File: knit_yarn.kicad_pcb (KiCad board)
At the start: 2 copper layers, 33.8 x 36.1 mm, 10 parts, among them SW1 SW_SPST

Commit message: components in place
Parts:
- added D5: LED, LED_SMD:LED_0603_1608Metric_Pad1.05x0.95mm_HandSolder, B.Cu at (107.4, 80.2)
- added D6: LED, LED_SMD:LED_0603_1608Metric_Pad1.05x0.95mm_HandSolder, B.Cu at (91.6, 80.5)
- added R5: TBD, Resistor_SMD:R_0603_1608Metric_Pad0.98x0.95mm_HandSolder, B.Cu at (110.0, 81.2)
- added R6: TBD, Resistor_SMD:R_0603_1608Metric_Pad0.98x0.95mm_HandSolder, B.Cu at (89.0, 81.5)
- D1, D2, D3, D4, R1, R2, R3, R4: moved to B.Cu
- moved R4 52.7 mm to (85.0, 86.5), turned to 90 degrees
- moved R2 52.1 mm to (85.0, 90.0), turned to -90 degrees
- moved D4 48.7 mm to (87.0, 75.5), turned to -135 degrees
- moved D2 46.8 mm to (88.2, 104.0), turned to 45 degrees
- moved D3 27.6 mm to (111.9, 74.1), turned to -45 degrees
- moved D1 25.7 mm to (112.6, 103.0), turned to 135 degrees
- moved R3 23.7 mm to (114.5, 84.8), turned to 90 degrees
- moved R1 22.6 mm to (114.5, 88.2), turned to -90 degrees
- moved SW1 2.00 mm to (99.5, 77.0)
- moved BT1 0.25 mm to (111.9, 93.8)
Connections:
- BT1 pad 1: +3V0 -> Net-(BT1-+)
- SW1 pad 1: unconnected-(SW1-A-Pad1) -> Net-(BT1-+)
- SW1 pad 2: unconnected-(SW1-B-Pad2) -> +3V0

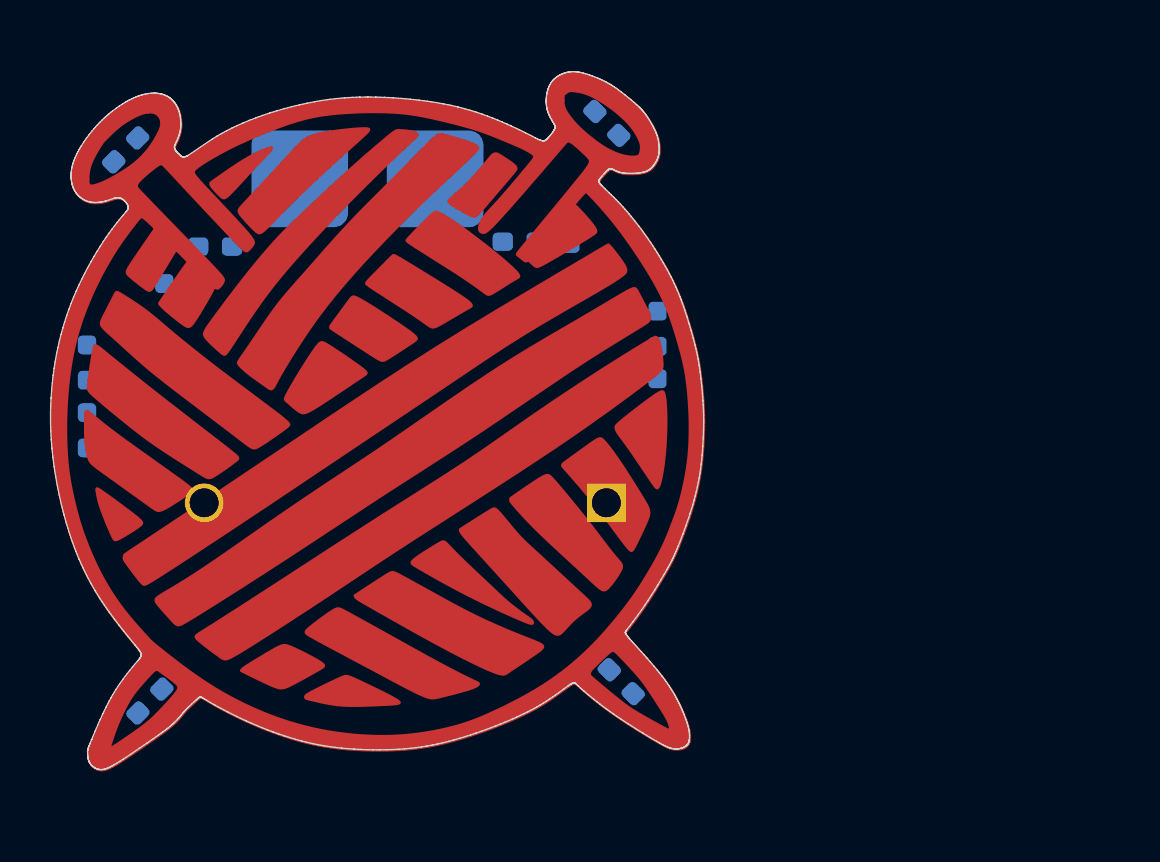
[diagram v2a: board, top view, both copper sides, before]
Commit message: back pour area
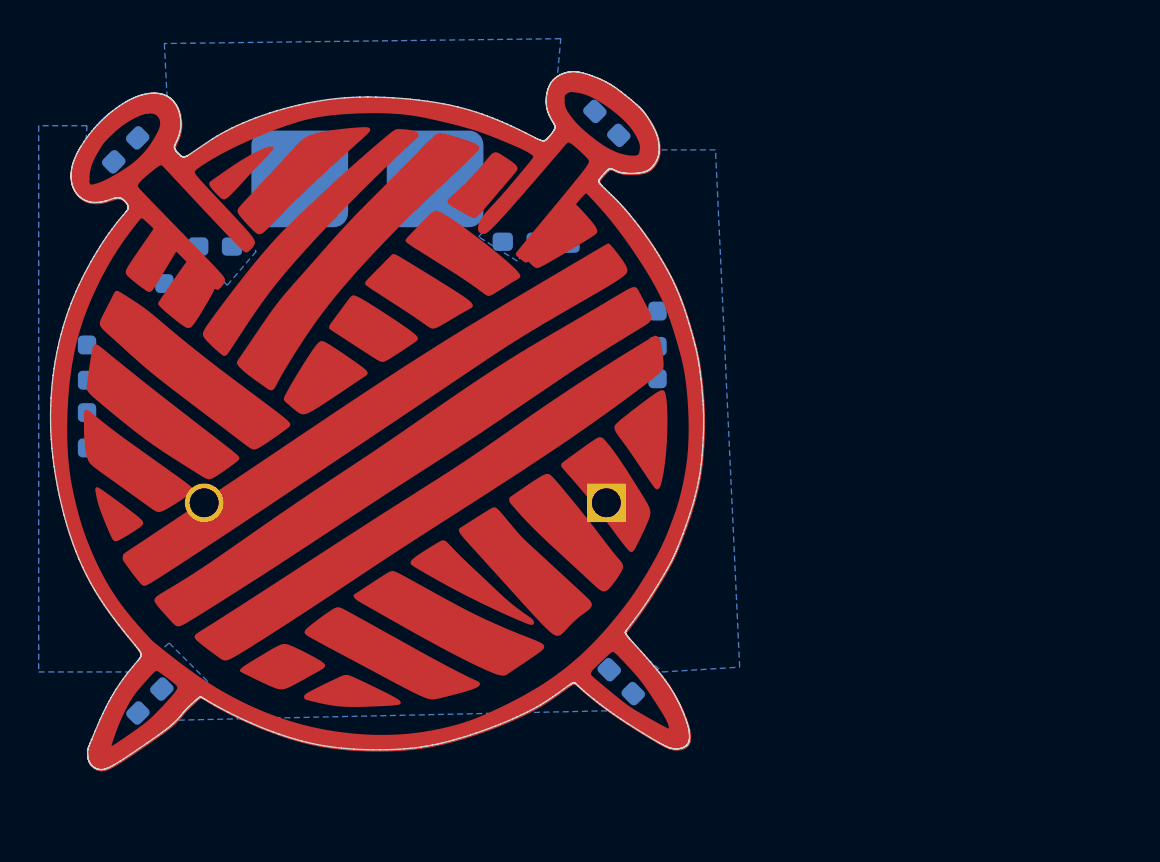
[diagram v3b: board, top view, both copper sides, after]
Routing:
- added copper zone on B.Cu, net GND
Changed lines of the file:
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@@
 		(layer "Edge.Cuts")
+	)
+	(zone
+		(net 2)
+		(net_name "GND")
+		(layer "B.Cu")
+		(hatch edge 0.5)
+		(connect_pads
+			(clearance 0.5)
+		)
+		(min_thickness 0.25)
+		(filled_areas_thickness no)
+		(fill yes
+			(thermal_gap 0.5)
+			(thermal_bridge_width 0.5)
+			(island_removal_mode 1)
+			(island_area_min 10)
+		)
+		(polygon
+			(pts
+				(xy 114.5 75.5) (xy 113.25 76.5) (xy 111.75 76) (xy 107.25 81.25) (xy 105.25 80) (xy 109 75.5) (xy 109.75 74.25)
+				(xy 109.25 72.5) (xy 109.5 69.75) (xy 89 70) (xy 89.25 75) (xy 89.25 76) (xy 93.75 80.75) (xy 92.25 82.5)
+				(xy 87.25 77.25) (xy 85.25 78) (xy 84.75 78) (xy 85 74.25) (xy 82.5 74.25) (xy 82.5 102.5) (xy 87.5 102.5)
+				(xy 89.25 101) (xy 91.25 103) (xy 89.25 105) (xy 112.25 104.5) (xy 110.25 102.5) (xy 112.5 100.5)
+				(xy 114.75 102.5) (xy 118.75 102.25) (xy 117.5 75.5)
+			)
+		)
 	)
 	(group ""

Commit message: fist draft
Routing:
- net +3V0: track 0.00 -> 71.5 mm
- net GND: track 0.00 -> 25.7 mm, vias 0 -> 2
- net Net-(BT1-+): track 0.00 -> 21.8 mm
- net Net-(D1-A): track 0.00 -> 14.9 mm
- net Net-(D2-A): track 0.00 -> 14.1 mm
- net Net-(D3-A): track 0.00 -> 11.6 mm
- net Net-(D4-A): track 0.00 -> 11.2 mm
- net Net-(D6-A): track 0.00 -> 1.79 mm
- net Net-(D5-A): track 0.00 -> 1.79 mm

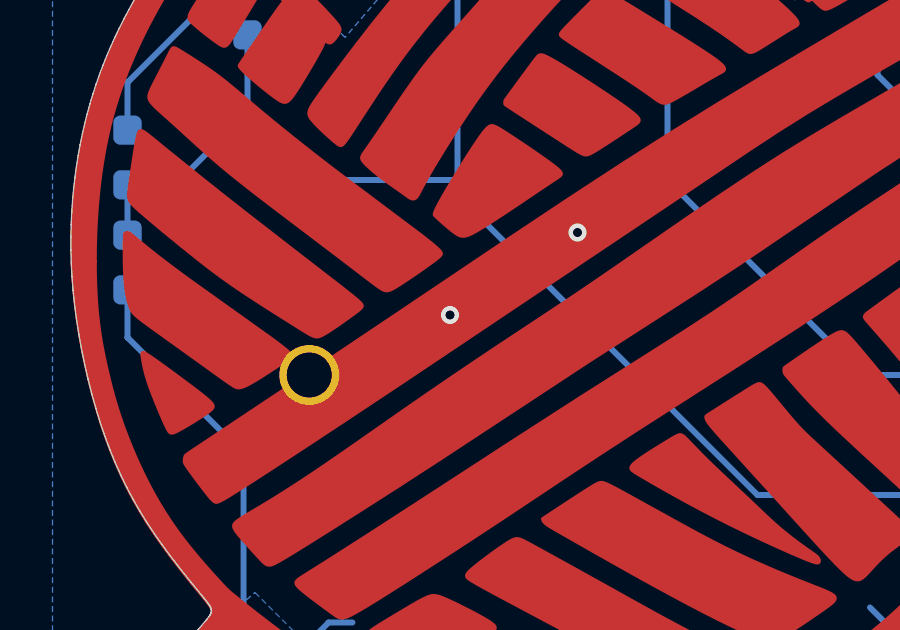
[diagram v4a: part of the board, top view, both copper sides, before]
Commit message: one via
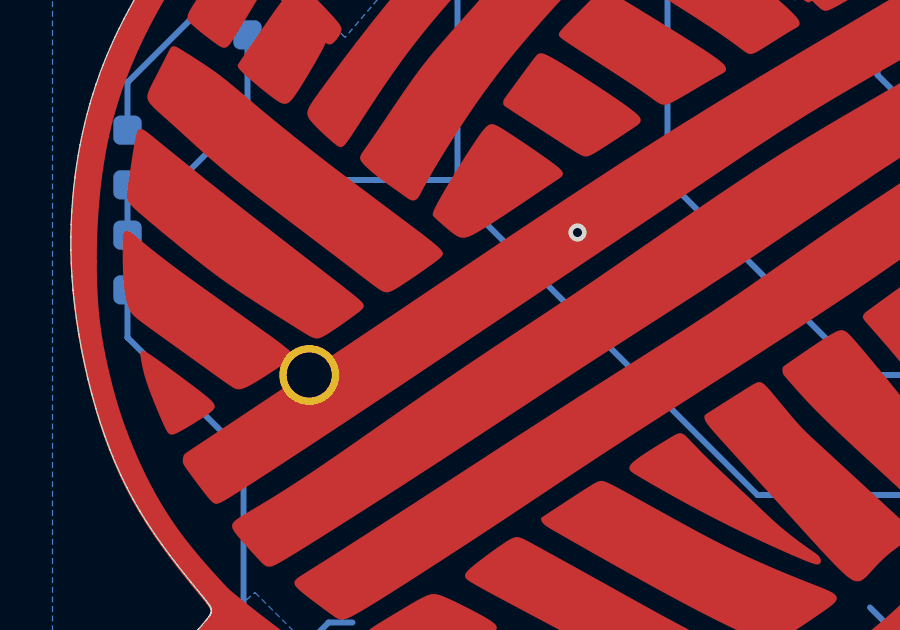
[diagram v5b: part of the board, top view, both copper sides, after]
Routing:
- net GND: vias 2 -> 1
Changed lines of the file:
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@@
-		(net 2)
-	)
-	(via
-		(at 95.75 91.75)
-		(size 0.6)
-		(drill 0.3)
-		(layers "F.Cu" "B.Cu")
-		(free yes)
 		(net 2)
 	)

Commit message: add silk screen
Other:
- board text added: "2025/05/12"
- board text added: "@borisnotes"
- board text added: "Stockholm, SWE"
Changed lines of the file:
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@@
 		(layer "Edge.Cuts")
+	)
+	(gr_text "@borisnotes"
+		(at 104 80.985 0)
+		(layer "B.SilkS")
+		(effects
+			(font
+				(size 1 1)
+				(thickness 0.1)
+			)
+			(justify left bottom mirror)
+		)
+	)
+	(gr_text "Stockholm, SWE"
+		(at 87 85.75 90)
+		(layer "B.SilkS")
+		(effects
+			(font
+				(size 1 1)
+				(thickness 0.1)
+			)
+			(justify left bottom mirror)
+		)
+	)
+	(gr_text "2025/05/12"
+		(at 112.5 88.75 315)
+		(layer "B.SilkS")
+		(effects
+			(font
+				(size 1 1)
+				(thickness 0.1)
+			)
+			(justify left bottom mirror)
+		)
 	)
 	(segment
